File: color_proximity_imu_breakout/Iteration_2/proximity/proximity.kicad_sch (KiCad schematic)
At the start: 11 parts, among them IC1 VL53L4CDV0DH_1, J1 Conn_01x10, J2 Conn_01x10, J4 Conn_01x05

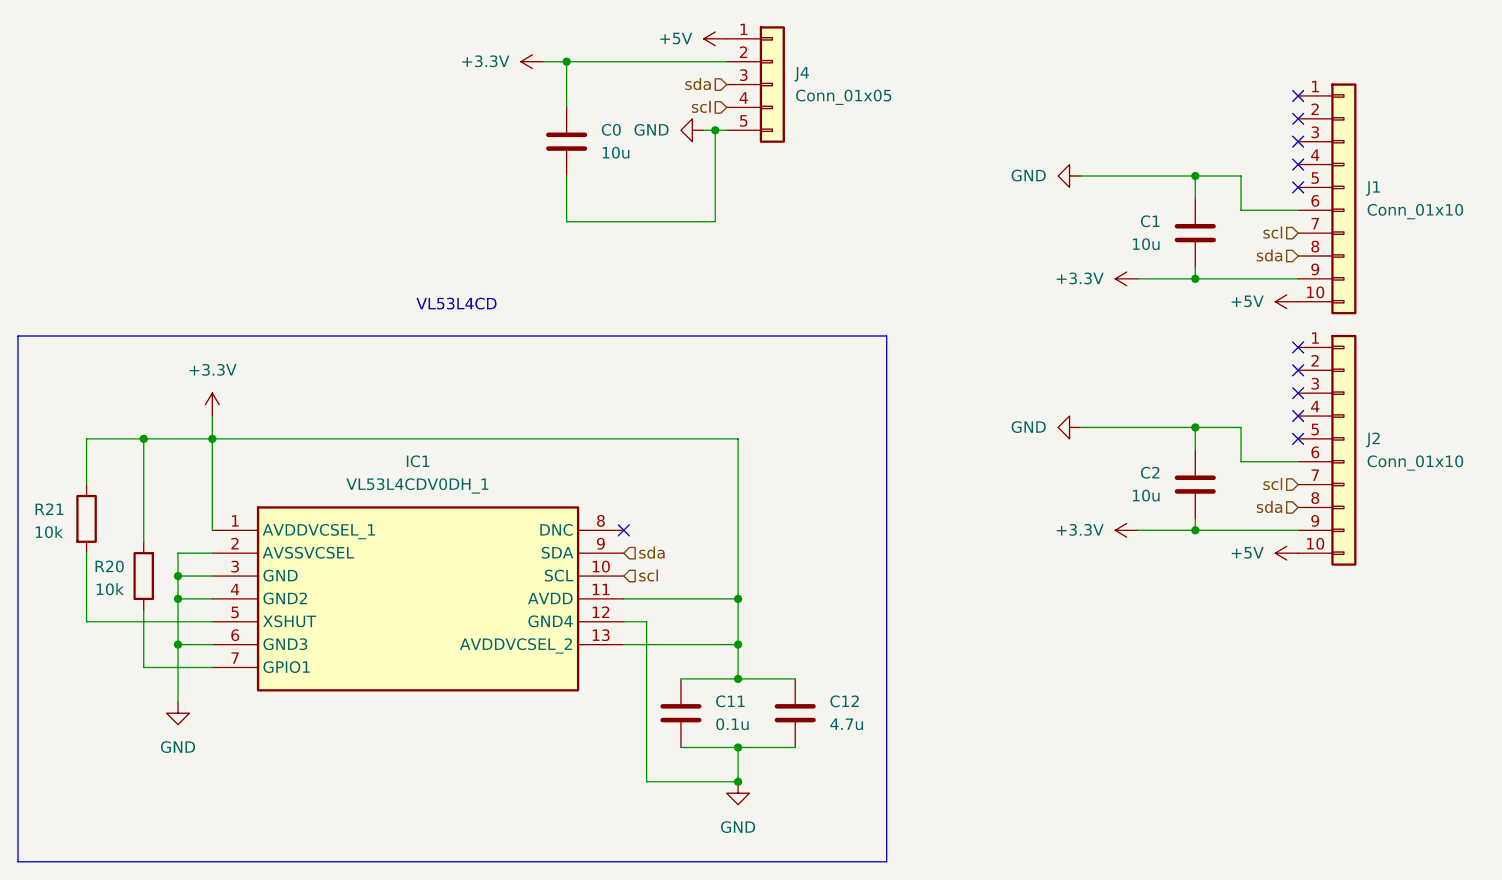
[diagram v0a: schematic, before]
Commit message: proximity board iteration 2 updated
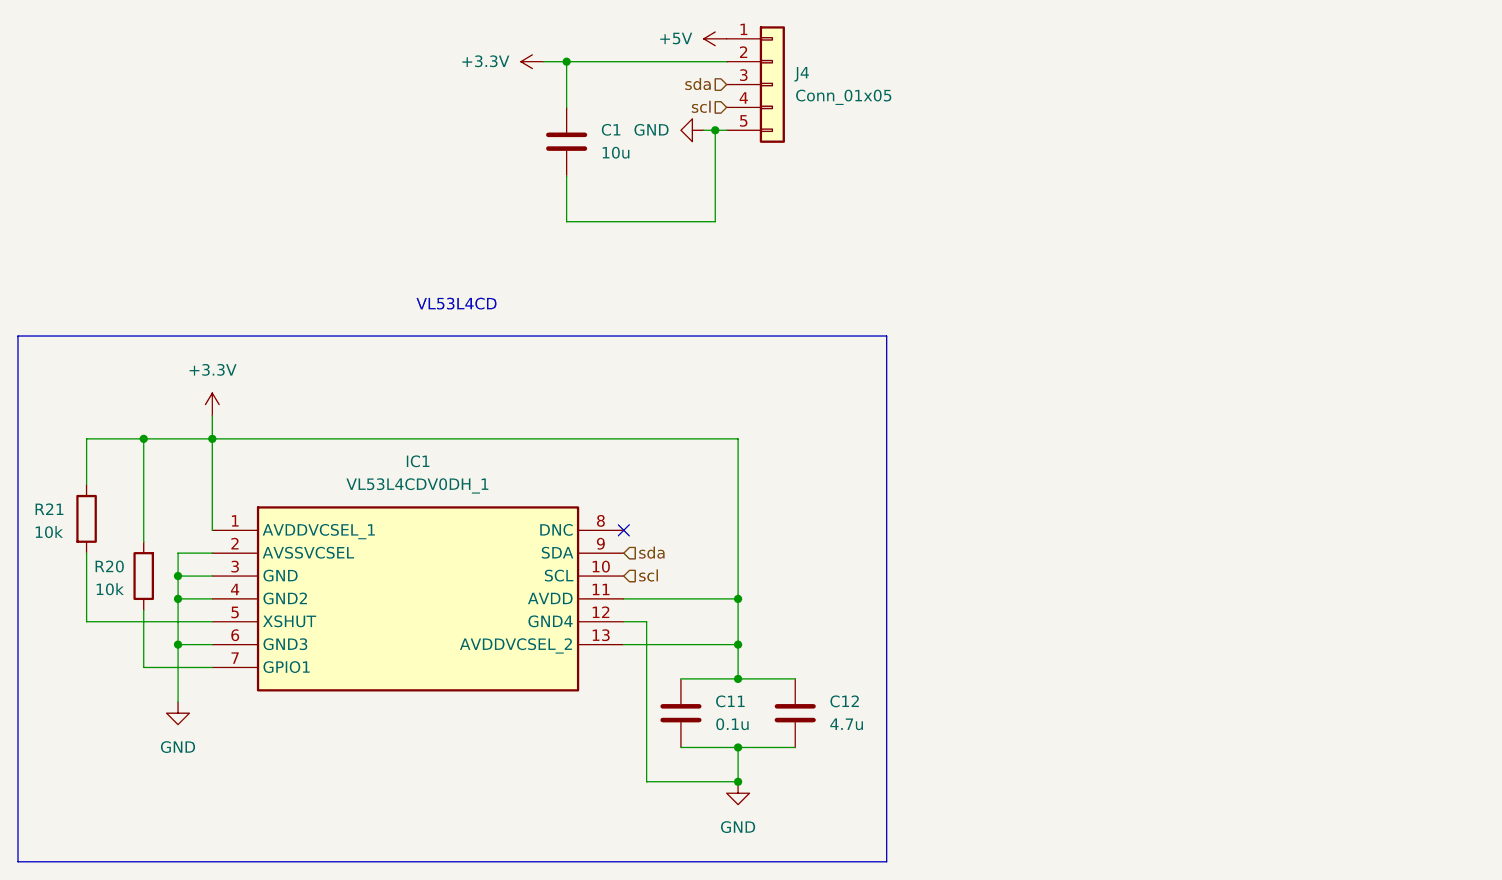
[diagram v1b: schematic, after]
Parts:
- removed C1, C2: 10u, Capacitor_SMD:C_0603_1608Metric_Pad1.08x0.95mm_HandSolder, symbol Device:C
- removed J1, J2: Conn_01x10, pcb_footprints:GT-B0502MSV27-10S1101, symbol Connector_Generic:Conn_01x10
- renumbered C0 to C1
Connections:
- no-connect marks 11 -> 1

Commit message: proximity board iteration 2 updated
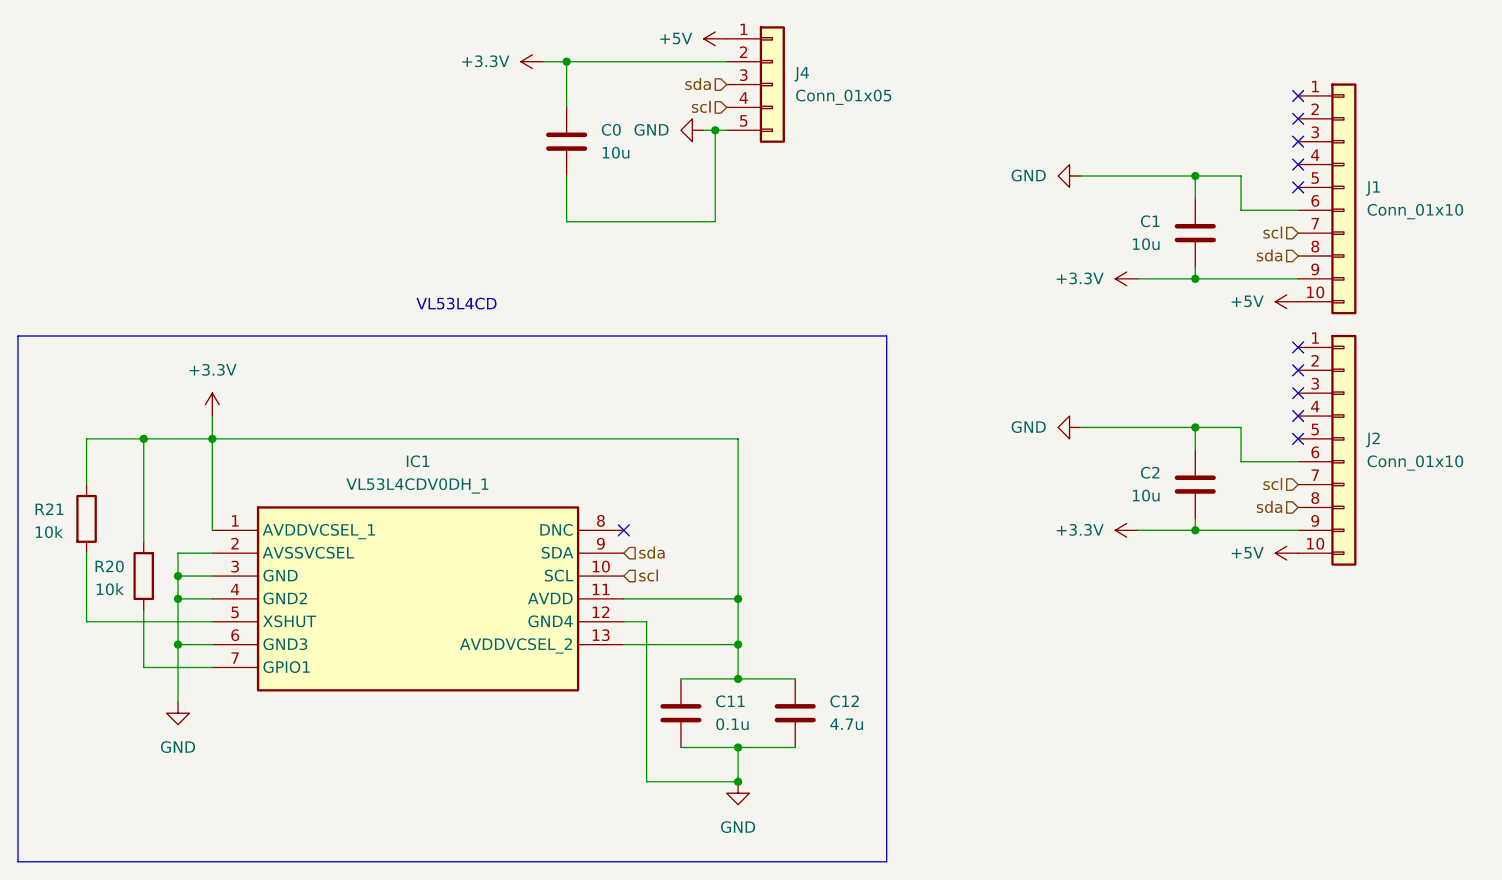
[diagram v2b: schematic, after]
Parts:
- added C1, C2: 10u, Capacitor_SMD:C_0603_1608Metric_Pad1.08x0.95mm_HandSolder, symbol Device:C
- added J1, J2: Conn_01x10, pcb_footprints:GT-B0502MSV27-10S1101, symbol Connector_Generic:Conn_01x10
- renumbered C1 to C0
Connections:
- net +3.3V: now also C1.2, C2.2, J1.9 (Pin_9), J2.9 (Pin_9)
- net +5V: now also J1.10 (Pin_10), J2.10 (Pin_10)
- net GND: now also C1.1, C2.1, J1.6 (Pin_6), J2.6 (Pin_6)
- net scl: now also J1.7 (Pin_7), J2.7 (Pin_7)
- net sda: now also J1.8 (Pin_8), J2.8 (Pin_8)
- no-connect marks 1 -> 11
